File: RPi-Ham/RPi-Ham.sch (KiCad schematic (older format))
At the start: 39 parts, among them J1 Conn_02x03_Counter_Clockwise, J2 RJ45, J3 Conn_02x03_Counter_Clockwise, J4 RJ45, J5 RJ45, J6 Conn_02x08_Counter_Clockwise, J7 RJ45, J8 Raspberry_Pi_2_3, J9 Conn_02x08_Counter_Clockwise, U1 PCM3060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

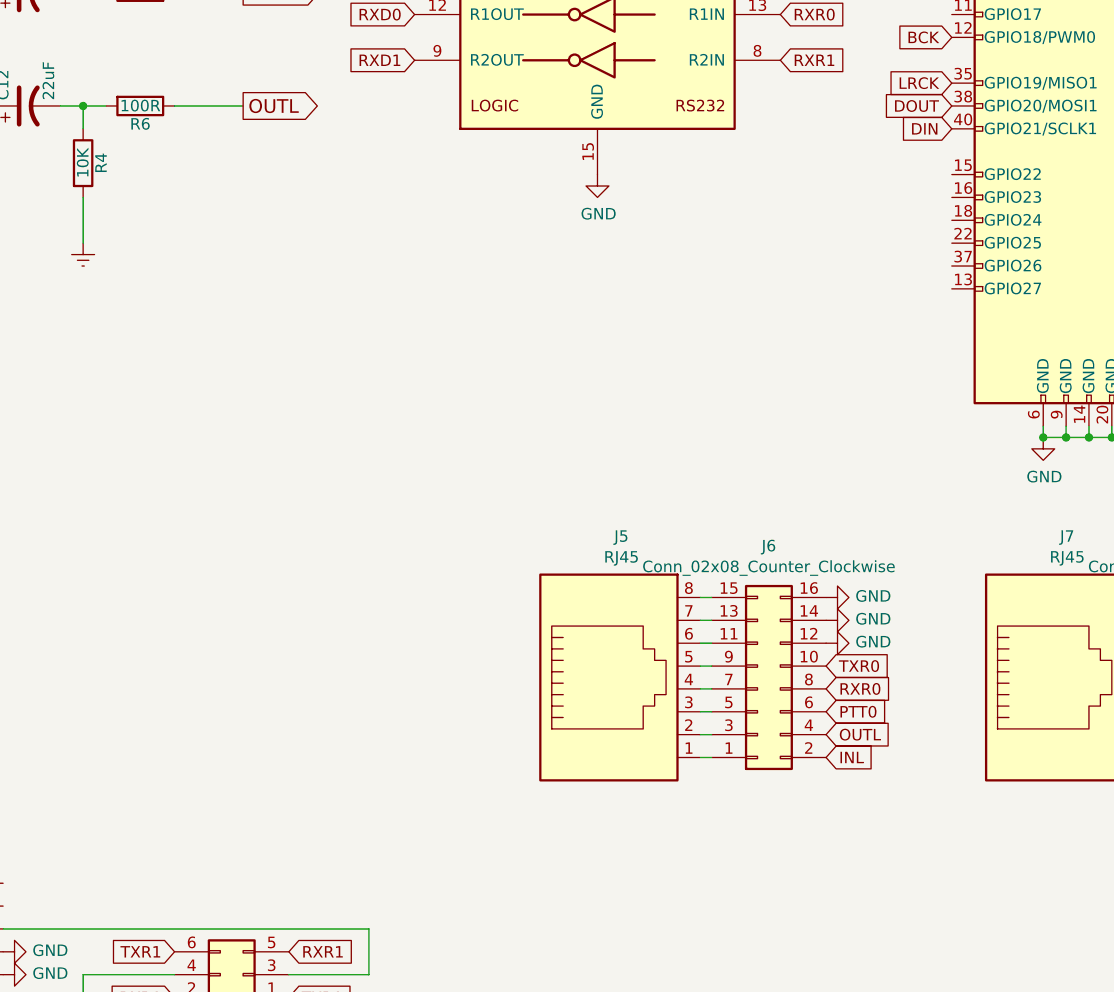
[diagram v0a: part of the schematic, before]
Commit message: Added PTT
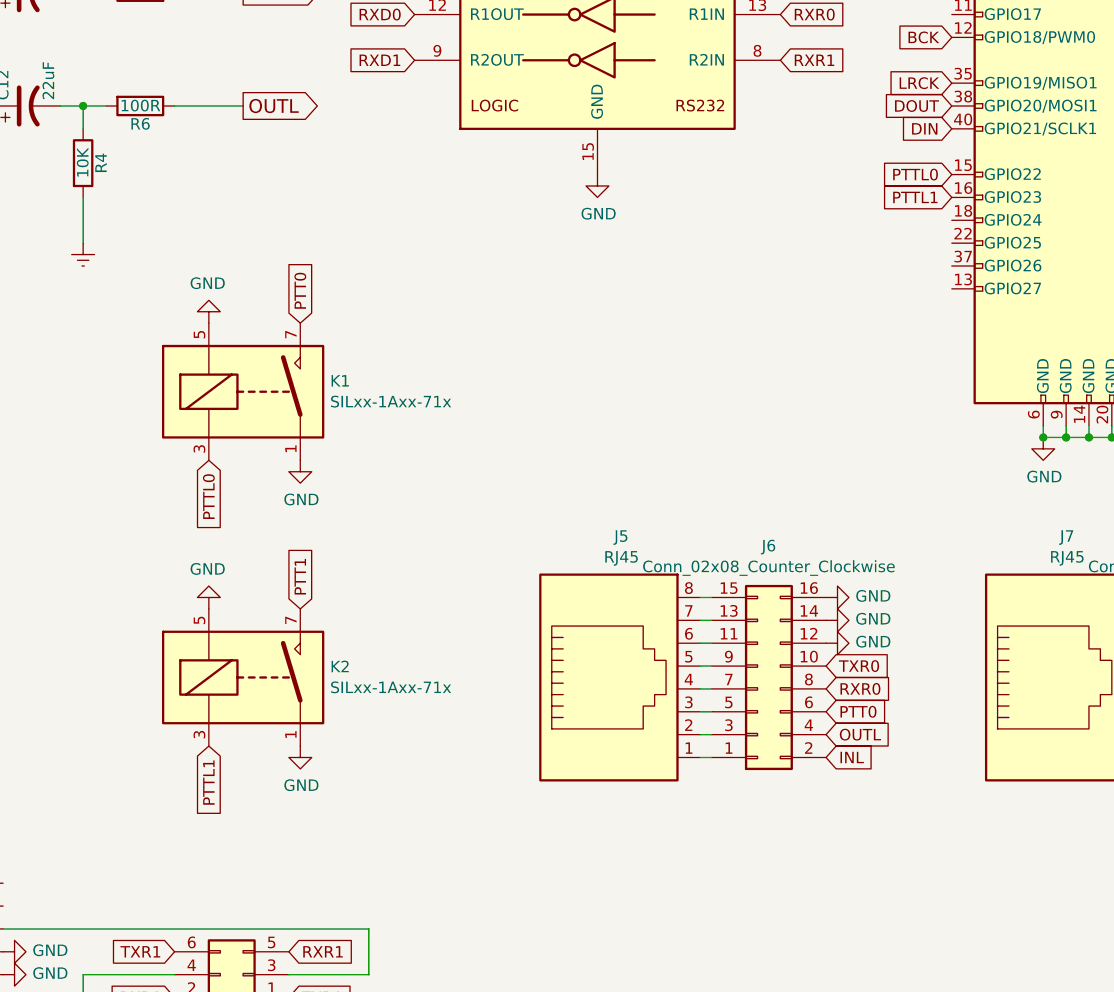
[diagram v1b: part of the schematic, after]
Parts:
- added K1, K2: SILxx-1Axx-71x, Relay_THT:Relay_SPST_StandexMeder_SIL_Form1A, symbol Relay:SILxx-1Axx-71x
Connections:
- net GND: now also K1.1, K1.5, K2.1, K2.5
- net PTT0: now also K1.7
- net PTT1: now also K2.7
- net PTTL0: now reaches J8.15 (GPIO22)
- net PTTL0: now also K1.3
- net PTTL1: now reaches J8.16 (GPIO23)
- net PTTL1: now also K2.3
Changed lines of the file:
@@
 EESchema Schematic File Version 4
 LIBS:RPi-Ham-cache
-LIBS:raspi_audio-cache
 EELAYER 26 0
 EELAYER END
@@
 Wire Wire Line
 	5400 7150 5400 7050
+$Comp
+L Relay:SILxx-1Axx-71x K1
+U 1 1 5D0F528F
+P 6150 4500
+F 0 "K1" H 6480 4546 50  0000 L CNN
+F 1 "SILxx-1Axx-71x" H 6480 4455 50  0000 L CNN
+F 2 "Relay_THT:Relay_SPST_StandexMeder_SIL_Form1A" H 6500 4450 50  0001 L CNN
+F 3 "https://standexelectronics.com/wp-content/uploads/datasheet_reed_relay_SIL.pdf" H 6150 4500 50  0001 C CNN
+	1    6150 4500
+	1    0    0    -1
+$EndComp
+$Comp
+L Relay:SILxx-1Axx-71x K2
+U 1 1 5D0F5325
+P 6150 5750
+F 0 "K2" H 6480 5796 50  0000 L CNN
+F 1 "SILxx-1Axx-71x" H 6480 5705 50  0000 L CNN
+F 2 "Relay_THT:Relay_SPST_StandexMeder_SIL_Form1A" H 6500 5700 50  0001 L CNN
+F 3 "https://standexelectronics.com/wp-content/uploads/datasheet_reed_relay_SIL.pdf" H 6150 5750 50  0001 C CNN
+	1    6150 5750
+	1    0    0    -1
+$EndComp
+$Comp
+L power:GND #PWR0132
+U 1 1 5D0F5C9C
+P 5950 4200
+F 0 "#PWR0132" H 5950 3950 50  0001 C CNN
+F 1 "GND" H 5955 4027 50  0000 C CNN
+F 2 "" H 5950 4200 50  0001 C CNN
+F 3 "" H 5950 4200 50  0001 C CNN
+	1    5950 4200
+	-1   0    0    1
+$EndComp
+$Comp
+L power:GND #PWR0133
+U 1 1 5D0F5DE7
+P 5950 5450
+F 0 "#PWR0133" H 5950 5200 50  0001 C CNN
+F 1 "GND" H 5955 5277 50  0000 C CNN
+F 2 "" H 5950 5450 50  0001 C CNN
+F 3 "" H 5950 5450 50  0001 C CNN
+	1    5950 5450
+	-1   0    0    1
+$EndComp
+Text GLabel 9200 3550 0    50   Input ~ 0
+PTTL0
+Text GLabel 9200 3650 0    50   Input ~ 0
+PTTL1
+Text GLabel 5950 4800 3    50   Input ~ 0
+PTTL0
+Text GLabel 5950 6050 3    50   Input ~ 0
+PTTL1
+$Comp
+L power:GND #PWR0134
+U 1 1 5D0F6193
+P 6350 6050
+F 0 "#PWR0134" H 6350 5800 50  0001 C CNN
+F 1 "GND" H 6355 5877 50  0000 C CNN
+F 2 "" H 6350 6050 50  0001 C CNN
+F 3 "" H 6350 6050 50  0001 C CNN
+	1    6350 6050
+	1    0    0    -1
+$EndComp
+$Comp
+L power:GND #PWR0135
+U 1 1 5D0F6207
+P 6350 4800
+F 0 "#PWR0135" H 6350 4550 50  0001 C CNN
+F 1 "GND" H 6355 4627 50  0000 C CNN
+F 2 "" H 6350 4800 50  0001 C CNN
+F 3 "" H 6350 4800 50  0001 C CNN
+	1    6350 4800
+	1    0    0    -1
+$EndComp
+Text GLabel 6350 4200 1    50   Input ~ 0
+PTT0
+Text GLabel 6350 5450 1    50   Input ~ 0
+PTT1
 $EndSCHEMATC
